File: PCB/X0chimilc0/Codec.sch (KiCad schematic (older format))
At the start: 1 part, among them U3 WM8994ECS-R

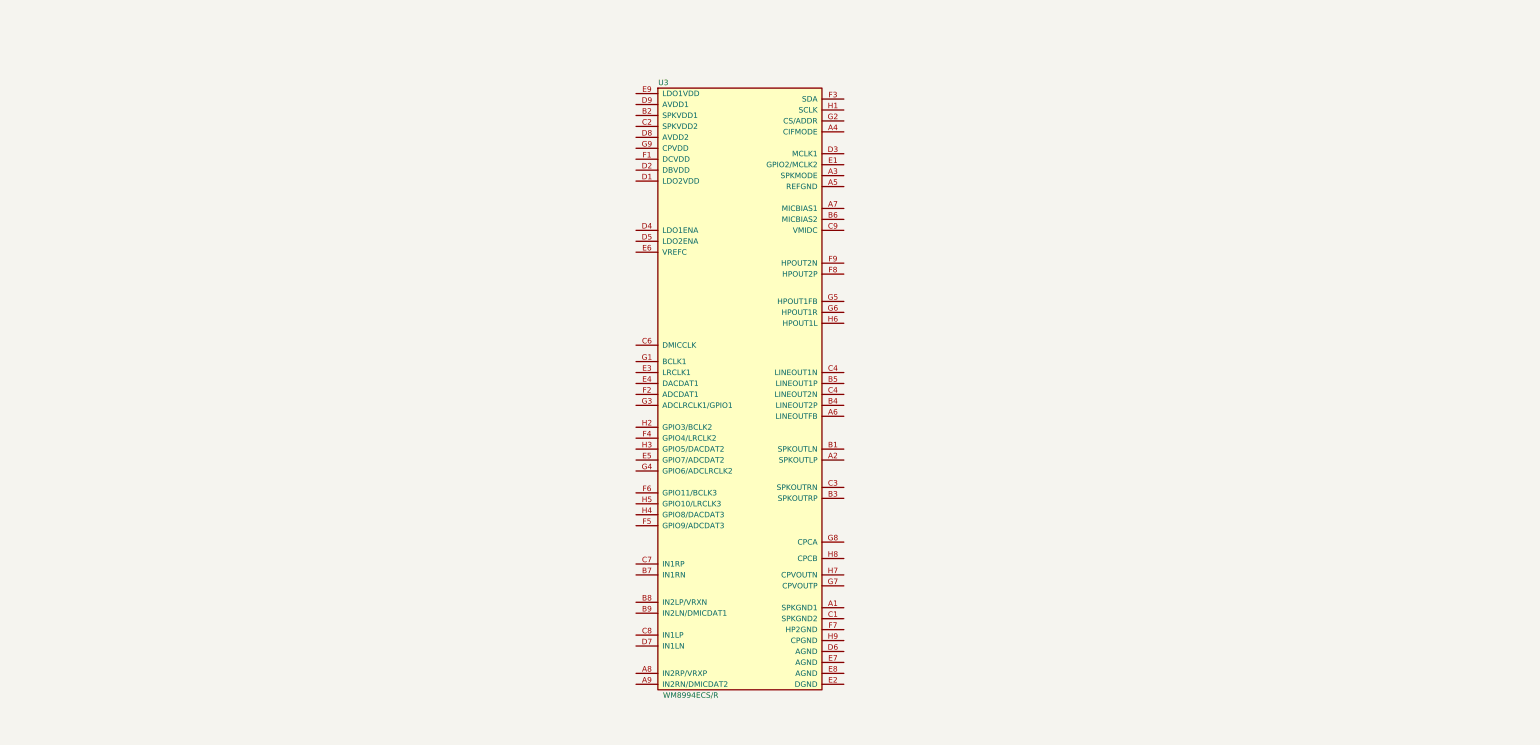
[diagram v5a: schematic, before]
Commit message: Aduio and USB C
audio codec mostly drawn
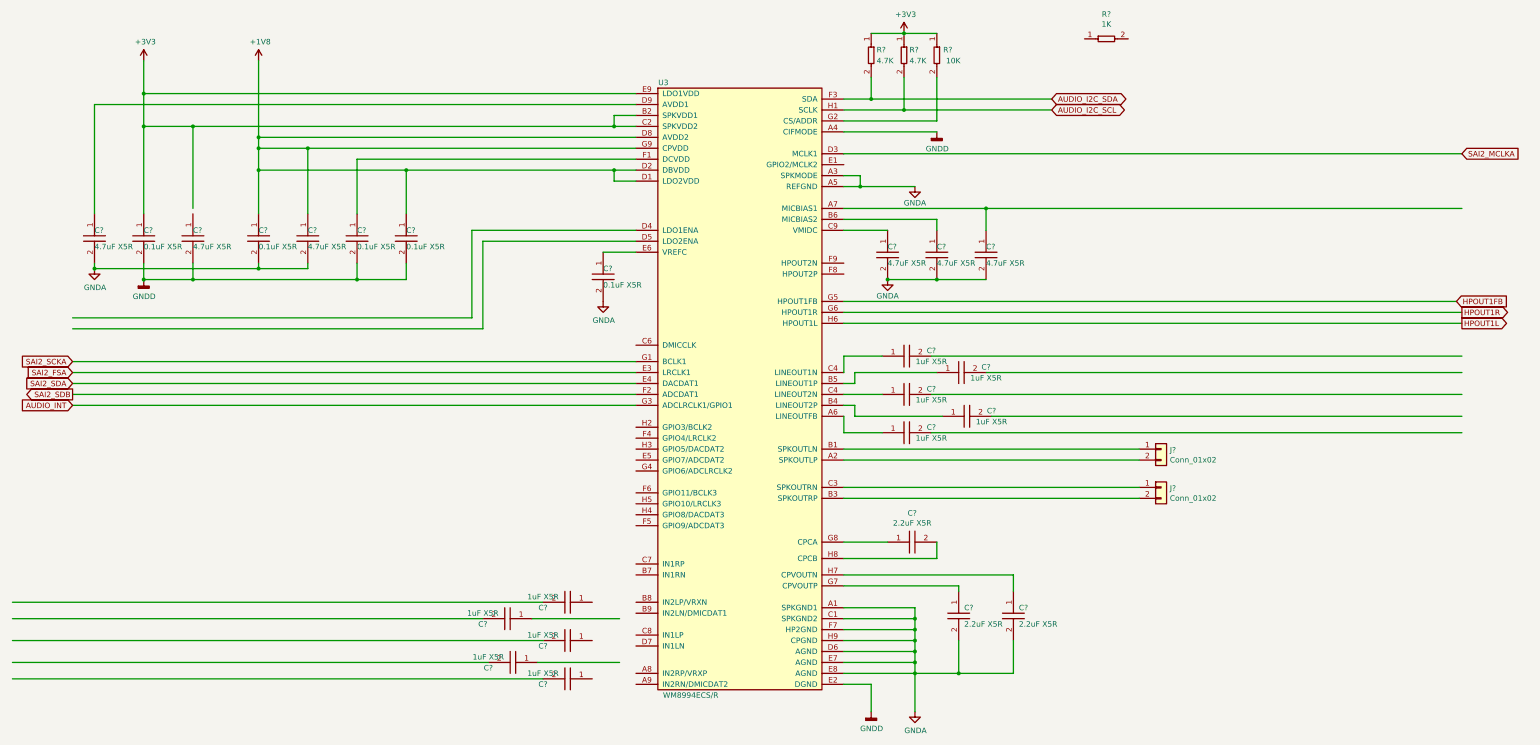
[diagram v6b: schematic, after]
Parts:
- added C? (x5): C0402C104K9PACTU, AVR-KiCAD-Lib-Resistors:R0402, symbol AVR-KiCAD-Lib-Capacitors:C0402C104K9PACTU
- added C? (x6): C0603C475K9PACTU, AVR-KiCAD-Lib-Capacitors:C0603, symbol AVR-KiCAD-Lib-Capacitors:C0603C475K9PACTU
- added C? (x3): CC0603KRX5R6BB225, AVR-KiCAD-Lib-Capacitors:C0603, symbol AVR-KiCAD-Lib-Capacitors:CC0603KRX5R6BB225
- added C? (x10): CC0603KRX5R7BB105, AVR-KiCAD-Lib-Capacitors:C0603, symbol AVR-KiCAD-Lib-Capacitors:CC0603KRX5R7BB105
- added J? (x2): Conn_01x02, Pin_Headers:Pin_Header_Straight_1x02_Pitch2.54mm, symbol Connector_Generic:Conn_01x02
- added R? (x2): RC0402FR-074K7L, AVR-KiCAD-Lib-Resistors:R0402, symbol AVR-KiCAD-Lib-Resistors:RC0402FR-074K7L
- added R?: RC0402FR-0710KL, AVR-KiCAD-Lib-Resistors:R0402, symbol AVR-KiCAD-Lib-Resistors:RC0402FR-0710KL
- added R?: RC0402FR-071KL, AVR-KiCAD-Lib-Resistors:R0402, symbol AVR-KiCAD-Lib-Resistors:RC0402FR-071KL
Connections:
- net labels added: +1V8, +3V3, AUDIO_I2C_SCL, AUDIO_I2C_SDA, AUDIO_INT, GNDA, GNDD, HPOUT1FB, HPOUT1L, HPOUT1R, SAI2_FSA, SAI2_MCLKA, SAI2_SCKA, SAI2_SDA, SAI2_SDB
- wire segments 0 -> 133

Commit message: DDR3L
Memory schematic for FPGA cloned from OrangeCrab R1.0 schematic, MCU memory started. Both need finishing.
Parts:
- removed C? (x2): CC0603KRX5R7BB105, AVR-KiCAD-Lib-Capacitors:C0603, symbol AVR-KiCAD-Lib-Capacitors:CC0603KRX5R7BB105
- removed R?: RC0402FR-071KL, AVR-KiCAD-Lib-Resistors:R0402, symbol AVR-KiCAD-Lib-Resistors:RC0402FR-071KL
- added C?: C0603C475K9PACTU, AVR-KiCAD-Lib-Capacitors:C0603, symbol AVR-KiCAD-Lib-Capacitors:C0603C475K9PACTU
- added R?: RC0402FR-074K7L, AVR-KiCAD-Lib-Resistors:R0402, symbol AVR-KiCAD-Lib-Resistors:RC0402FR-074K7L
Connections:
- net labels added: AUDIO_IN_LEFT_N, AUDIO_IN_LEFT_P, AUDIO_IN_RIGHT_N, AUDIO_IN_RIGHT_P, LEFT_N_OUT, LEFT_P_OUT, LINOUT_FB, RIGHT_N_OUT, RIGHT_P_OUT
- wire segments 133 -> 135
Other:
- note added: "Audio_Int"
- note added: "Digital\nAudio \nInterface\nTo MCU"
- note added: "Headphone Outout"
- note added: "PG10"
- note added: "PI4"
- note added: "PI5"
- note added: "PI6"
- note added: "PI7"
- note added: "Stereo Output, Left Channel"
- note added: "Stereo Output, Right Channel"
- note added: "WM8994ECS/R Audio Codec"
- moved on the sheet: C?, J?, R?, U3

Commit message: USB C DDR3L MCU
more with MCU and USB C and DDR3L
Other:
- note added: "Default I2C Address: 0011010"
- note added: "LEFT Speaker"
- note added: "PD12"
- note added: "PD13"
- note added: "RIGHT Speaker"
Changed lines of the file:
@@
 $Descr A3 16535 11693
 encoding utf-8
-Sheet 7 10
+Sheet 7 11
 Title ""
 Date ""
@@
 Text Notes 5800 1850 0    236  ~ 47
 WM8994ECS/R Audio Codec
+Text Notes 14100 3400 0    50   ~ 0
+PD13
+Text Notes 14100 3500 0    50   ~ 0
+PD12
+Text Notes 13800 3300 0    50   ~ 0
+Default I2C Address: 0011010
+Text Notes 11900 6650 0    50   ~ 0
+LEFT Speaker
+Text Notes 11900 7000 0    50   ~ 0
+RIGHT Speaker
 $EndSCHEMATC
